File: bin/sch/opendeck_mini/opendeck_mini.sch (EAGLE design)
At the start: 137 parts, among them Q1 BSS314PEH6327XTSA1, Q2 NTGD3148N, Q5 NTGD3148N, U1 6N137, U2 AT90USB1286, U3 MC14067BDWR2G-SO24W, U4 74HC165, U5 74HC165, Y1 16MHz

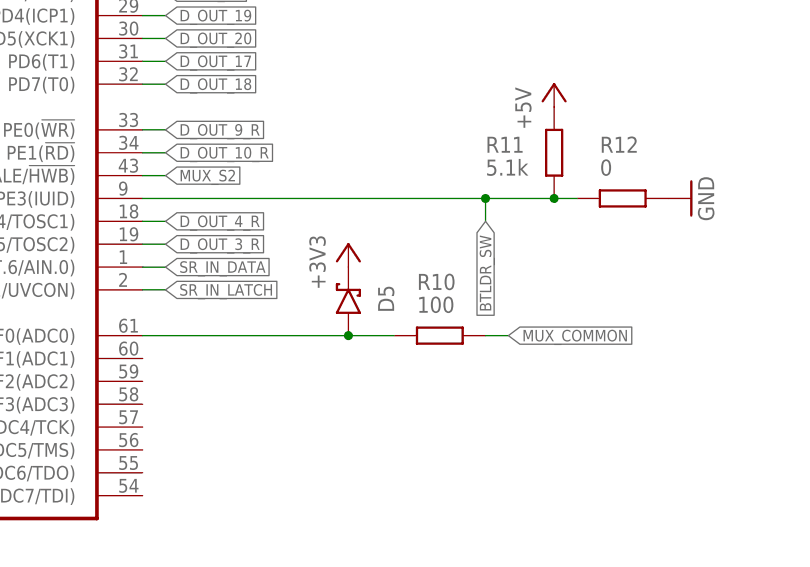
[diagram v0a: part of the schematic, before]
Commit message: targets/opendeck_mini: remove schottky diode on adc input
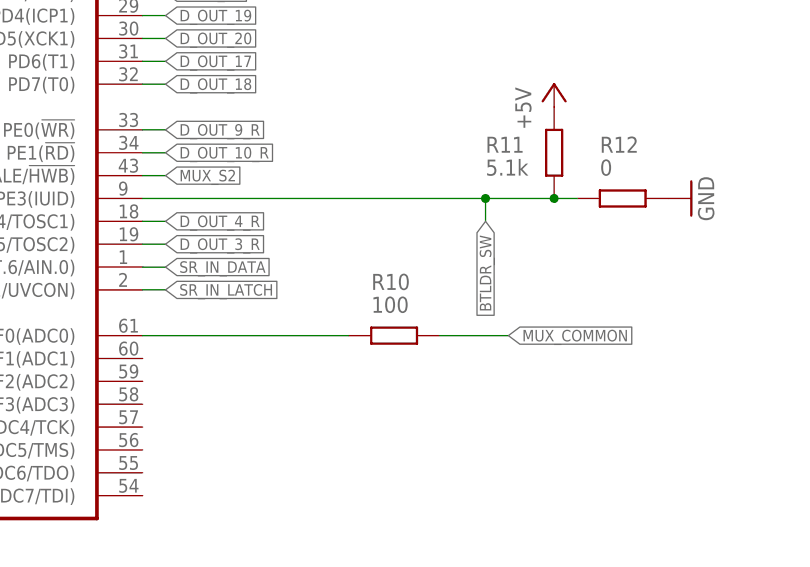
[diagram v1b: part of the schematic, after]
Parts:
- removed D5: BAT46-SOT23, igor_lbr:BAT46-SOT23
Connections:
- net +3V3: no longer D5.C
- net N$20: no longer D5.A
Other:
- moved on the sheet: R10
